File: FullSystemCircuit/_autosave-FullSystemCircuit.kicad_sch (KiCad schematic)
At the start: 34 parts, among them J1 HVD, K1 Gigavac GV200, K2 Gigavac GV200, SW1 GLVMS, SW10 Left, SW11 Right, SW2 TS_Activate, SW3 BSPD, SW4 IMD, SW5 TSMS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

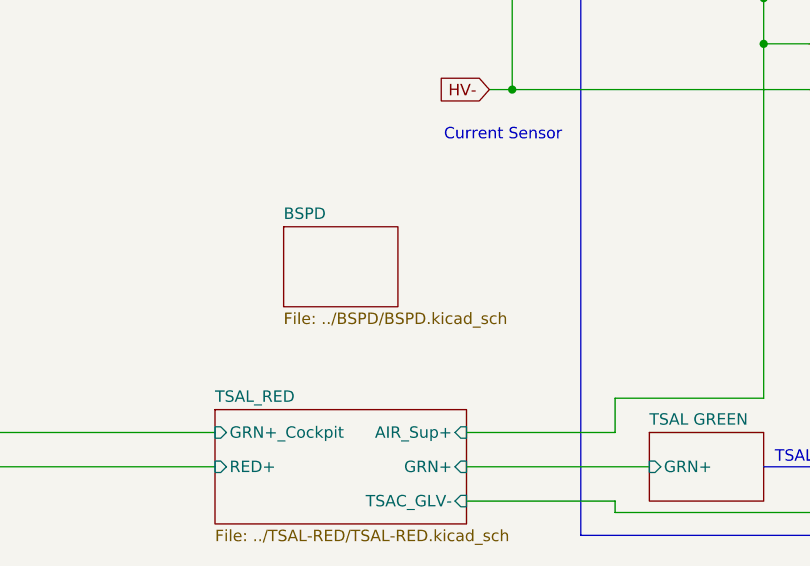
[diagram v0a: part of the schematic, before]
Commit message: added hierarchichal labels for hierarchical sheet compatibility
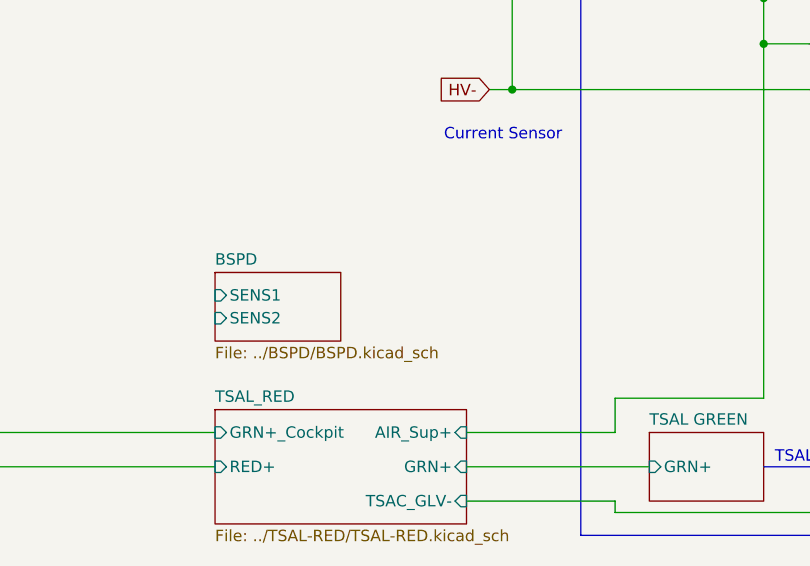
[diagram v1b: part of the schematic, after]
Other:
- sheet BSPD ports: added SENS1, SENS2; removed none
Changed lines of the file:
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@@
 	)
 	(sheet
-		(at 127 234.95)
-		(size 12.7 8.89)
+		(at 119.38 240.03)
+		(size 13.97 7.62)
 		(exclude_from_sim no)
 		(in_bom yes)
@@
 		)
 		(property "Sheetname" "BSPD"
-			(at 127 234.2384 0)
+			(at 119.38 239.3184 0)
 			(effects
 				(font
@@
 		)
 		(property "Sheetfile" "../BSPD/BSPD.kicad_sch"
-			(at 127 244.4246 0)
+			(at 119.38 248.2346 0)
 			(effects
 				(font
@@
 			)
 		)
+		(pin "SENS1" input
+			(at 119.38 242.57 180)
+			(effects
+				(font
+					(size 1.27 1.27)
+				)
+				(justify left)
+			)
+		)
+		(pin "SENS2" input
+			(at 119.38 245.11 180)
+			(effects
+				(font
+					(size 1.27 1.27)
+				)
+				(justify left)
+			)
+		)
